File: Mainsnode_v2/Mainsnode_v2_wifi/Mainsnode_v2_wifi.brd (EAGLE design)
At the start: 72.6 x 47.1 mm, 70 parts, among them IC1 7805T, J2 WIRE_HOLE-14AWG, J3 WIRE_HOLE-14AWG, J4 HOLE, J5 HOLE, J6 HOLE, J7 HOLE, K1 S216S01F, Q1 STGD5NB120SZT4, Q2 3.579545MHz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

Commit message: Start route wifi board
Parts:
- removed C5, C6: C1uF, resistor:C0805
- removed IC1: 7805T, adafruit:TO220H
- removed JP1: (no value), pinhead:2X04
- removed L2, L3: EMI_SUPRESSION_FERRITE_BEAD, powercube:L1806
- removed TP_ADE_CF, TP_ADE_CS, TP_ADE_IRQ, TP_ADE_ZX, TP_MISO, TP_MOSI, TP_SCK: PTR1PAD1-13, testpad:P1-13
- added C18, C19: C10uF, resistor:C0805
- added IC2: LD117AS50TR, v-reg:SOT223
- added R7: R10K, resistor:R0805
- added U$3: ESP8266, tigorcustom:ESP8266
- added U$4, U$5: BLM18BB151SN1, tigorcustom:L0603
- U$1: device SparkFun-Boards:ARDUINO_PRO_MINI -> tigorcustom:ARDUINO_PRO_MINI
- moved JP2 396.6 mm to (24.1, 10.5), turned to 180 degrees
- moved J3 394.8 mm to (53.7, 41.0)
- moved J2 386.1 mm to (46.7, 41.0)
- moved TP_V2P 369.7 mm to (43.5, 45.4), turned to 90 degrees
- moved C17 357.6 mm to (55.2, 33.0), turned to 90 degrees
- moved R15 353.1 mm to (57.5, 33.0), turned to 270 degrees
- moved R14 349.4 mm to (59.7, 34.0), turned to 90 degrees
- moved C16 341.6 mm to (58.7, 37.5)
- moved TP_V1N 338.5 mm to (46.4, 45.4), turned to 90 degrees
- moved L4 333.9 mm to (54.3, 28.9)
- moved R13 333.5 mm to (58.7, 39.7), turned to 180 degrees
- moved TP_V1P 314.2 mm to (49.2, 45.4), turned to 90 degrees
- moved C15 308.2 mm to (52.1, 32.1)
- moved R12 300.1 mm to (52.1, 34.3)
- moved R11 288.8 mm to (69.2, 36.2), turned to 90 degrees
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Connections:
- net 3V3: now also U$3.VCC; no longer JP1.7
- net 5V: now also C19.1, IC2.4, R7.1; no longer C6.1, IC1.3
- net ADE_CF: now also U$1.8; no longer TP_ADE_CF.TP, U$1.20
- net ADE_CS: no longer TP_ADE_CS.TP
- net ADE_IRQ: now also R7.2, U$1.6; no longer TP_ADE_IRQ.TP, U$1.18
- net ADE_ZX: now also U$1.7; no longer TP_ADE_ZX.TP, U$1.19
- net DBG_RXI: now also U$1.20; no longer U$1.8
- net DBG_TXO: now also U$1.19; no longer U$1.7
- net GND: now also C18.2, C19.2, IC2.1, U$3.GND; no longer C5.2, C6.2, IC1.2, JP1.2
- net LOAD_NEUTRAL: now also U$4.1; no longer L2.P$1
- net MISO: no longer TP_MISO.TP
- net MOSI: no longer TP_MOSI.TP
- net N$14: now also U$4.2; no longer L2.P$2
- net N$15: now also U$5.2; no longer L3.P$2
- net RELAY_CTRL: now also U$1.18; no longer U$1.6
- net RXI: now also U$3.TXD; no longer JP1.1
- net SCK: no longer TP_SCK.TP
- net TXO: now also U$3.RXD; no longer JP1.8
- net VDC: now also C18.1, IC2.3; no longer C5.1, IC1.1
- net WALL_NEUTRAL: now also U$5.1; no longer L3.P$1
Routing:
- net GND: track 0.00 -> 148.4 mm, vias 0 -> 12
- net ADE_ZX: track 0.00 -> 47.6 mm
- net ADE_IRQ: track 0.00 -> 47.0 mm
- net ADE_CF: track 0.00 -> 45.8 mm
- net VDC: track 0.00 -> 39.3 mm, vias 0 -> 3
- net TXO: track 0.00 -> 35.7 mm
- net 3V3: track 0.00 -> 28.2 mm
- net RXI: track 0.00 -> 25.4 mm
- net N$12: track 0.00 -> 23.8 mm
- net ADE_CS_5V: track 0.00 -> 22.9 mm
- net SCK_5V: track 0.00 -> 22.7 mm
- net MISO_5V: track 0.00 -> 22.4 mm
- net MOSI_5V: track 0.00 -> 22.1 mm
- net N$1: track 0.00 -> 22.0 mm
- net WALL_NEUTRAL: track 0.00 -> 20.7 mm
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
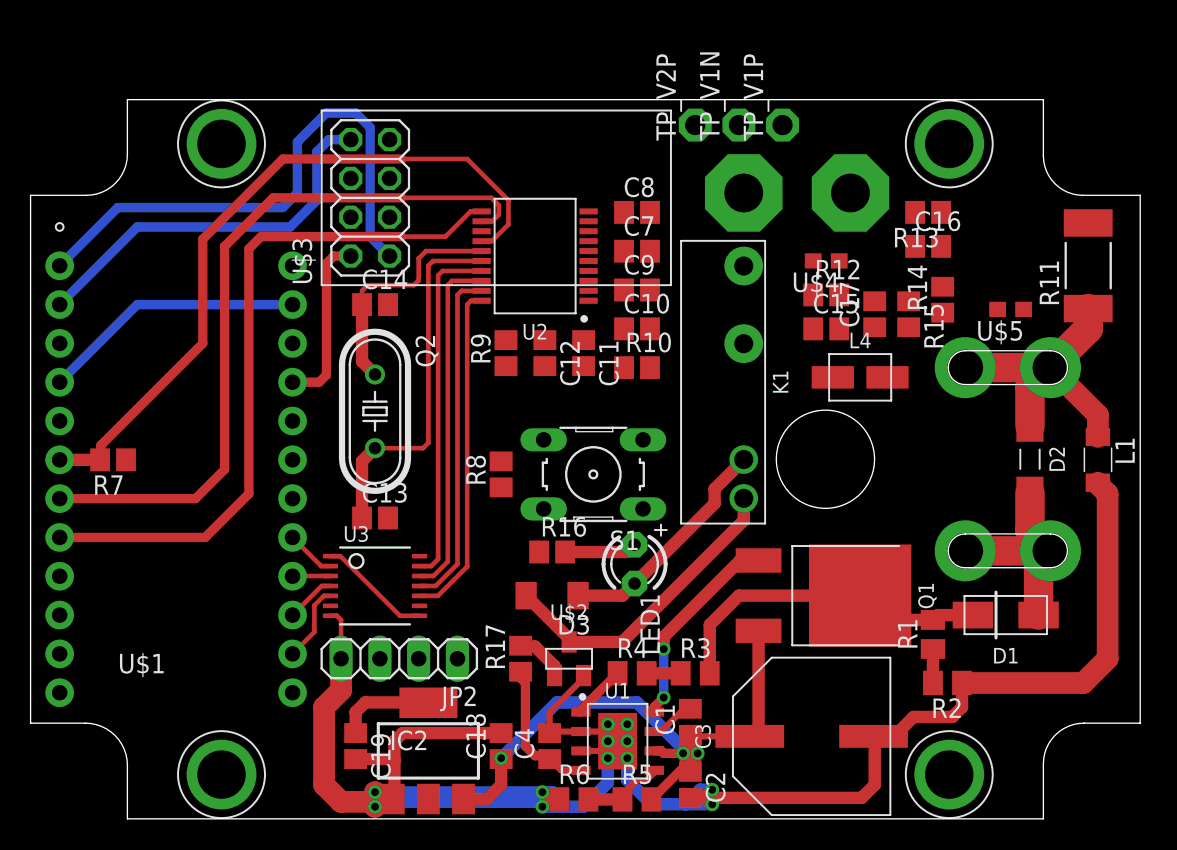
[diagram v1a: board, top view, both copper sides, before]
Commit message: Finish route wifi board and order component
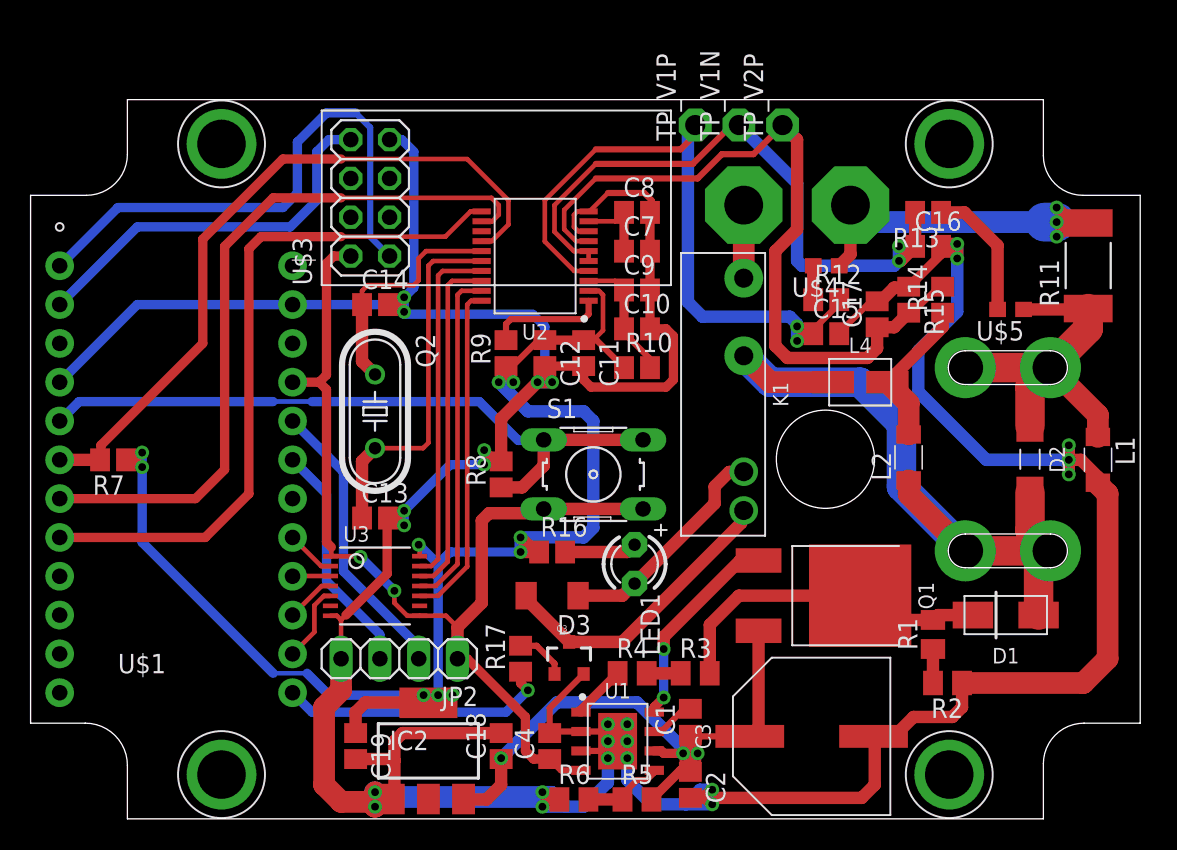
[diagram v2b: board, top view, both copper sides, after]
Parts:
- removed U$2: FDV301N, powercube:SOT-23
- added L2: BLM31PG330SN1, resistor:L3216C
- added Q3: MMBT2222A, SparkFun-DiscreteSemi:SOT23-3
- R17: value R100K -> R220
- moved TP_V1P 5.71 mm to (43.5, 45.4)
- moved TP_V2P 5.71 mm to (49.2, 45.4)
- moved R15 0.95 mm to (57.5, 34.0)
- moved J2 0.79 mm to (46.7, 40.2)
- moved J3 0.79 mm to (53.7, 40.2)
- moved K1 0.79 mm to (46.7, 27.8)
- moved C15 0.32 mm to (52.1, 31.8)
- moved R12 0.32 mm to (52.1, 34.0)
- moved U$4 0.32 mm to (52.1, 36.2)
- moved L4 0.32 mm to (54.3, 28.6)
- moved C17 0.16 mm to (55.4, 33.0)
- turned S1 to 0 degrees
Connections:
- new net N$19: Q3.1, R17.2
- net 3V3: no longer R17.1
- net GND: now also Q3.2; no longer U$2.2
- net N$17: now also L2.2
- net N$18: now also Q3.3; no longer U$2.3
- net RELAY_CTRL: now also R17.1, U$1.13; no longer R17.2, U$1.18, U$2.1
- net WALL_PHASE: now also L2.1
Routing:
- net GND: track 148.4 -> 286.1 mm, vias 12 -> 25
- net 5V: track 6.41 -> 95.7 mm, vias 0 -> 10
- net V2P: track 0.00 -> 49.2 mm
- net USER_RELAY_CTRL: track 0.00 -> 44.8 mm
- net V1P: track 0.00 -> 44.1 mm, vias 0 -> 2
- net V1N: track 0.00 -> 42.5 mm, vias 0 -> 2
- net 3V3: track 28.2 -> 67.0 mm, vias 0 -> 2
- net WALL_PHASE: track 14.5 -> 49.4 mm
- net LOAD_NEUTRAL: track 0.00 -> 25.2 mm, vias 0 -> 3
- net DBG_RXI: track 0.00 -> 19.0 mm
- net DBG_TXO: track 0.00 -> 15.4 mm
- net RELAY_CTRL: track 3.40 -> 17.9 mm, vias 0 -> 1
- net N$17: track 0.00 -> 10.0 mm
- net N$15: track 0.00 -> 8.78 mm
- net N$13: track 0.00 -> 8.35 mm
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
